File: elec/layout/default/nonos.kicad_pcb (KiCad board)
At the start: 2 copper layers, 60 parts, among them CN1 HRSHirose_DF40C_100DS_0_4V51, CN2 HRSHirose_DF40C_100DS_0_4V51, Q1 MOSFET, U1 STUSB4500QTR, U2 _Texas_Instruments_SN74LVC1G0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, U3 _Texas_Instruments_TAS5825MRH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, U4 Texas_Instruments_TPS56637RPAR

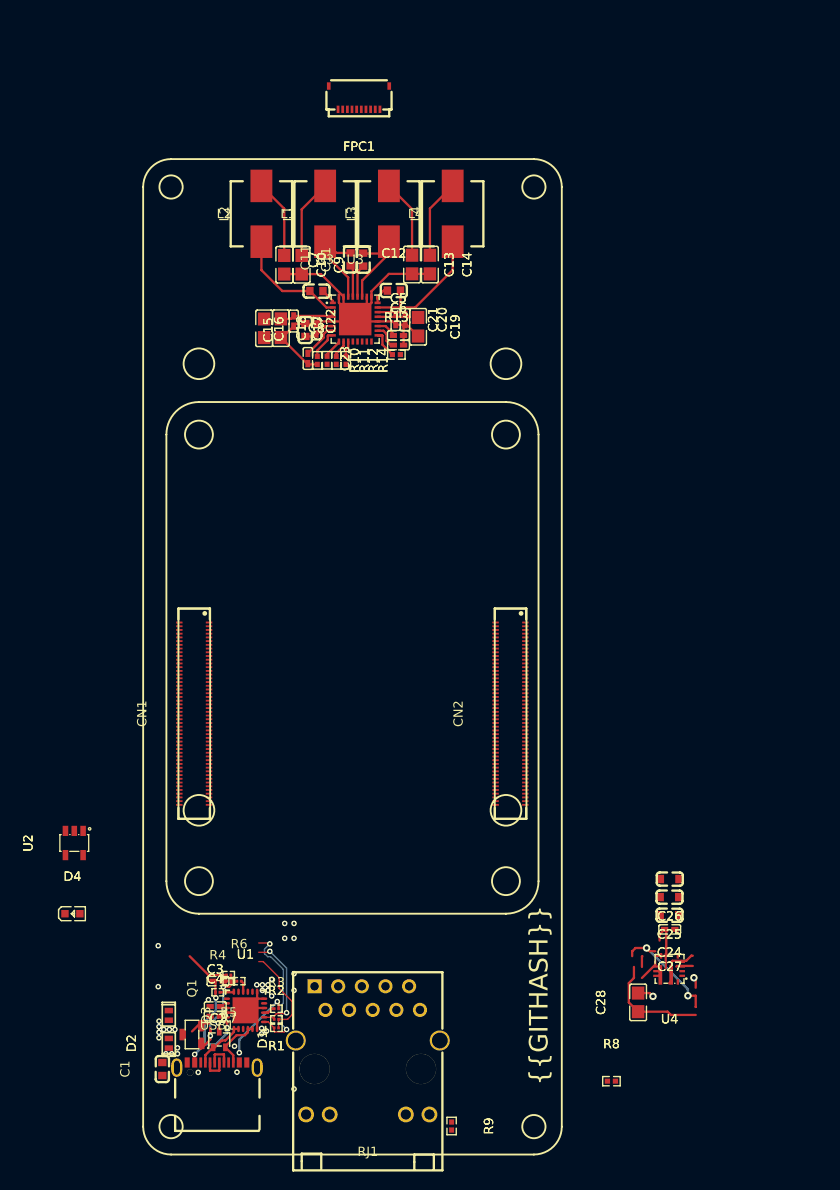
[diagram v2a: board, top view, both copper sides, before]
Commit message: add hat interface to nonos board
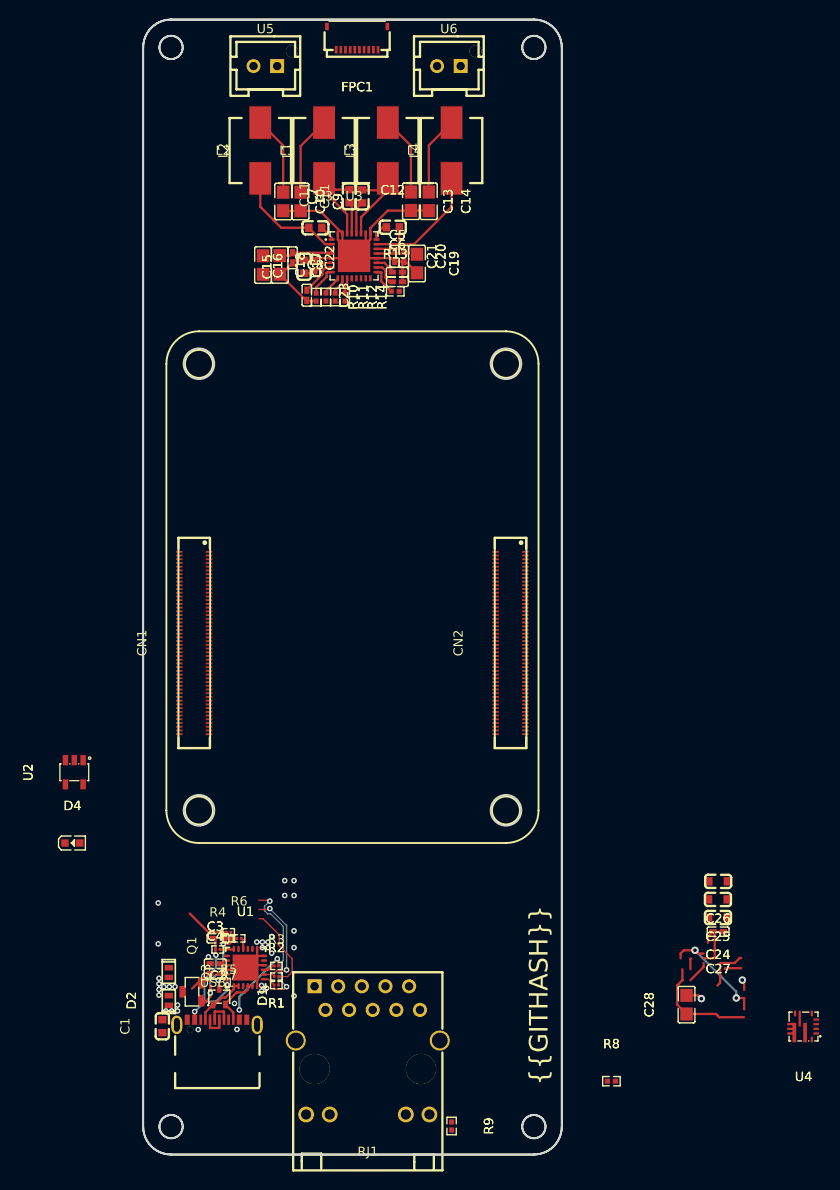
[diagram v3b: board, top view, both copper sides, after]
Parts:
- added U5: JST_Sales_America_B02B_XASK_1_ALFSN, lcsc:CONN-TH_B02B-XASK-1-A-LF-SN, F.Cu at (129.7, 49.4)
- added U6: JST_Sales_America_B02B_XASK_1_ALFSN, lcsc:CONN-TH_B02B-XASK-1-A-LF-SN, F.Cu at (149.5, 49.4)
- C5: value 1µF ±10% 25V X5R -> (none)
- C6: value (none) -> 1µF ±10% 25V X5R
- moved U4 15.7 mm to (187.6, 152.6)
- moved D4 7.60 mm to (109.0, 132.9)
- moved CN1 7.60 mm to (122.1, 111.4)
- moved CN2 7.60 mm to (156.1, 111.4)
- moved U2 7.60 mm to (109.2, 125.3)
- moved C17 6.80 mm to (131.3, 70.8)
- moved C18 6.80 mm to (129.5, 70.8)
- moved C5 6.80 mm to (143.9, 71.6)
- moved L1 6.80 mm to (136.0, 58.5)
- moved C10 6.80 mm to (131.7, 64.0)
- moved C13 6.80 mm to (145.4, 63.9)
- moved C9 6.80 mm to (133.5, 64.0)
- moved L2 6.80 mm to (129.2, 58.5)
- moved L3 6.80 mm to (142.9, 58.5)
- moved L4 6.80 mm to (149.8, 58.5)
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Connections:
- net amplifier-signal renamed net-2
- net amplifier-signal-1 renamed net-1
- net amplifier-signal-3 renamed net-3
- net pins[27] renamed processor.hdi_b-pins[27]
- net pins[38] renamed processor.hdi_b-pins[38]
- net pins[39] renamed processor.hdi_b-pins[39]
- net pins[46] renamed processor-pins[46]
- net processor-signal-7 renamed processor-pins[27]
- net processor-signal-8 renamed processor-pins[38]
- net processor.hdi_b-pins[28] renamed pins[28]
- C10 pad 2: amplifier-net -> amplifier-net-6
- C11 pad 1: amplifier-net-12 -> amplifier-net-4
- C11 pad 2: amplifier-net-9 -> amplifier-net-12
- C12 pad 1: amplifier-net-10 -> amplifier-net-1
- C12 pad 2: amplifier-net-4 -> amplifier-net-2
- C13 pad 2: amplifier-net -> amplifier-net-6
- C14 pad 2: amplifier-net -> amplifier-net-6
- C15 pad 2: amplifier-net -> amplifier-net-6
- C16 pad 2: amplifier-net -> amplifier-net-6
- C17 pad 2: amplifier-net -> amplifier-net-6
- C18 pad 2: amplifier-net -> amplifier-net-6
- C19 pad 2: amplifier-net -> amplifier-net-6
- C20 pad 2: amplifier-net -> amplifier-net-6
- C21 pad 2: amplifier-net -> amplifier-net-6
- C22 pad 2: amplifier-net -> amplifier-net-6
- C23 pad 1: amplifier-net-6 -> amplifier-net-8
- C23 pad 2: amplifier-net -> amplifier-net-6
- C5 pad 2: amplifier-net -> amplifier-net-6
- C6 pad 1: amplifier-net-3 -> amplifier-net-11
- C6 pad 2: amplifier-net -> amplifier-net-6
- C7 pad 1: amplifier-net-11 -> amplifier-net-5
- C7 pad 2: amplifier-net-5 -> amplifier-net
- C8 pad 1: amplifier-net-8 -> amplifier-net-10
- C8 pad 2: amplifier-net-1 -> amplifier-net-3
- C9 pad 1: amplifier-signal-2 -> net
- C9 pad 2: amplifier-net -> amplifier-net-6
- CN1 pad 15: signal-3 -> signal-6
- CN1 pad 17: signal-5 -> signal-7
- CN1 pad 19: pins[37] -> processor-signal-1
- CN1 pad 20: processor-signal-6 -> processor-pins[39]
- CN1 pad 23: pins[45] -> processor-signal-5
- CN1 pad 25: processor-signal-2 -> processor-signal-3
- CN1 pad 27: signal-2 -> signal-4
- CN1 pad 28: signal-6 -> signal-3
- CN1 pad 73: processor-signal-1 -> pins[54]
- CN1 pad 77: processor-signal-5 -> processor-pins[46]-1
- CN1 pad 78: processor-signal-4 -> processor-signal
- CN1 pad 82: signal-4 -> signal-5
- CN1 pad 85: processor-signal-3 -> processor-signal-2
- CN1 pad 86: processor-pins[28] -> processor-signal-4
- CN1 pad 87: processor-signal -> processor-signal-6
- D4 pad 1: net -> net-4
- FPC1 pad 10: signal-4 -> signal-5
- FPC1 pad 7: signal-2 -> signal-4
- FPC1 pad 8: signal-5 -> signal-7
- FPC1 pad 9: signal-3 -> signal-6
- L1 pad 1: amplifier-net-5 -> amplifier-net
- L1 pad 2: amplifier-signal-2 -> net
- L2 pad 1: amplifier-net-1 -> amplifier-net-3
- L3 pad 1: amplifier-net-9 -> amplifier-net-12
- L4 pad 1: amplifier-net-4 -> amplifier-net-2
- R10 pad 1: amplifier-net-2 -> amplifier-net-9
- R10 pad 2: amplifier-net -> amplifier-net-6
- R12 pad 1: signal-7 -> signal
- R13 pad 1: signal-6 -> signal-3
- R14 pad 1: signal -> signal-2
- R4 pad 2: pd_controller-net-3 -> pd_controller-net-2
- R6 pad 2: pd_controller-net-2 -> pd_controller-net-3
- R8 pad 2: rj45-net -> rj45-net-1
- R9 pad 2: rj45-net-1 -> rj45-net
- RJ1 pad 12: rj45-net -> rj45-net-1
- RJ1 pad 13: rj45-net-1 -> rj45-net
- U1 pad 16: pd_controller-net-2 -> pd_controller-net-3
- U1 pad 18: pd_controller-net-3 -> pd_controller-net-2
- U2 pad 4: net -> net-4
- U3 pad 1: amplifier-net-8 -> amplifier-net-10
- U3 pad 10: signal-7 -> signal
- U3 pad 11: signal -> signal-2
- U3 pad 17: signal-6 -> signal-3
- U3 pad 18: amplifier-net-3 -> amplifier-net-11
- U3 pad 2: amplifier-net-1 -> amplifier-net-3
- U3 pad 20: amplifier-net -> amplifier-net-6
- U3 pad 23: amplifier-net-4 -> amplifier-net-2
- U3 pad 24: amplifier-net-10 -> amplifier-net-1
- U3 pad 25: amplifier-net -> amplifier-net-6
- U3 pad 26: amplifier-net -> amplifier-net-6
- U3 pad 27: amplifier-net-9 -> amplifier-net-12
- U3 pad 28: amplifier-net-12 -> amplifier-net-4
- U3 pad 29: amplifier-net-11 -> amplifier-net-5
- U3 pad 30: amplifier-net-5 -> amplifier-net
- U3 pad 31: amplifier-net -> amplifier-net-6
- U3 pad 32: amplifier-net -> amplifier-net-6
- U3 pad 33: amplifier-net -> amplifier-net-6
- U3 pad 5: amplifier-net -> amplifier-net-6
- U3 pad 7: amplifier-net-6 -> amplifier-net-8
- U3 pad 8: amplifier-net-2 -> amplifier-net-9
- USB1 pad 5: pd_controller.USB_CONNECTOR-net-1 -> pd_controller.USB_CONNECTOR-net
- USB1 pad 6: pd_controller.USB_CONNECTOR-net -> pd_controller.USB_CONNECTOR-net-1
- USB1 pad 7: pd_controller.USB_CONNECTOR-net-1 -> pd_controller.USB_CONNECTOR-net
- USB1 pad 8: pd_controller.USB_CONNECTOR-net -> pd_controller.USB_CONNECTOR-net-1
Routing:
- net amplifier-net-6: track 12.4 -> 50.8 mm
- net amplifier-net-2: track 50.8 -> 14.6 mm
- net lv-1: track 20.0 -> 0.00 mm
- net lv: track 0.00 -> 20.0 mm, vias 1 -> 2
- net amplifier-net-11: track 14.6 -> 2.78 mm
- net pd_controller-net: track 12.1 -> 0.66 mm, vias 2 -> 0
- net pd_controller-net-1: track 1.22 -> 12.1 mm, vias 0 -> 2
- net amplifier-net-12: track 2.12 -> 10.8 mm
- net net: track 0.00 -> 8.52 mm
- net amplifier-signal-2: track 8.50 -> 0.00 mm
- net amplifier-net-3: track 4.03 -> 12.4 mm
- net amplifier-net-1: track 10.2 -> 2.12 mm
- net amplifier-net-5: track 10.8 -> 3.41 mm
- net amplifier-net: track 3.41 -> 10.2 mm
- net signal-5: track 3.34 -> 0.00 mm
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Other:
- board outline added: 45 x 122 mm

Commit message: builds working
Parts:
- removed USB1: TYPE_C_16PIN_2MD073, lcsc:USB-C-SMD_TYPE-C-6PIN-2MD-073
- added C29: 100nF ±10% 16V X7R, lcsc:C0402, F.Cu at (158.3, 151.4)
- added C30: 100pF ±5% 50V C0G, lcsc:C0402, F.Cu at (152.3, 150.9)
- added D5: , lcsc:LED0805-R-RD, F.Cu at (0.00, 0.00)
- added D6: , lcsc:LED0805-R-RD, F.Cu at (0.00, -5.00)
- added D7: , lcsc:LED0805-R-RD, F.Cu at (0.00, -10.0)
- added L5: 3.3µH ±20% 4A 73mΩ, lcsc:IND-SMD_L4.0-W4.0, F.Cu at (155.7, 155.4)
- added R15: 22kΩ ±1% 62.5mW, lcsc:R0402, F.Cu at (152.4, 152.0)
- added R16: 8.2kΩ ±1% 62.5mW, lcsc:R0402, F.Cu at (158.6, 154.7)
- added R17: 68kΩ ±1% 62.5mW, lcsc:R0402, F.Cu at (158.6, 156.8)
- added R18: 100kΩ ±1% 62.5mW, lcsc:R0402, F.Cu at (152.4, 153.2)
- added R19: 5.1kΩ ±1% 62.5mW, lcsc:R0402, F.Cu at (0.00, -15.0)
- added U7: _Texas_Instruments_TPS56637RPAR, lcsc:VQFN-HR-10_L3.0-W3.0_RPA, F.Cu at (155.6, 150.6)
- C10, C13, C14: value (none) -> 680nF ±10% 50V X7R
- C11, C12, C8: value (none) -> 470nF ±10% 50V X7R
- C18, C19: value (none) -> 22µF ±20% 25V X5R
- C2: value (none) -> 100nF ±10% 10V X5R; footprint lcsc:C0402 -> lcsc:C0201
- C20, C21, C22, C27: value (none) -> 100nF ±10% 16V X7R
- C23, C5: value (none) -> 1µF ±10% 25V X5R
- C24, C25, C26: value (none) -> 4.7µF ±10% 25V X5R; footprint lcsc:C0603 -> lcsc:C0805
- C3, C4: value (none) -> 1µF ±20% 6.3V X5R; footprint lcsc:C0402 -> lcsc:C0201
- D4: value 2.7V -> (none); footprint lcsc:LED0603-RD_WHITE -> lcsc:LED0805-R-RD
- L1, L3, L4: value (none) -> 10µH ±20% 4.5A 68mΩ
- Q1: footprint lcsc:SOT-23-3_L2.9-W1.3-P1.90-LS2.4-BR -> lcsc:SOT-23-3_L2.9-W1.3-P1.90-LS2.4-BR-1
- R1: value (none) -> 1kΩ ±1% 50mW
- R12, R13, R14: value (none) -> 10kΩ ±1% 62.5mW
- R2: value 4.64kΩ ±1% 50mW -> 4.7kΩ ±1% 50mW
- R3: value (none) -> 4.7kΩ ±1% 50mW
- R8: value 453Ω ±1% 62.5mW -> 470Ω ±1% 62.5mW
- R9: value (none) -> 470Ω ±1% 62.5mW
- U4: value Texas_Instruments_TPS56637RPAR -> _HCTL_HC_TYPE_C_24P_VS9_3_5A_F1_1_04; footprint lcsc:VQFN-HR-10_L3.0-W3.0_RPA -> lcsc:USB-C-SMD_HC-TYPE-C-24P-VS9.3-5A-F1.1-04; moved to B.Cu
- moved U4 48.7 mm to (139.1, 157.6), turned to -90 degrees
- moved R8 37.2 mm to (130.1, 163.5), turned to -90 degrees
- moved C25 23.3 mm to (155.8, 144.5)
- moved C26 23.3 mm to (155.8, 142.6)
- moved C27 23.3 mm to (155.8, 148.0)
- moved C24 23.3 mm to (155.8, 146.5)
- moved C28 23.3 mm to (152.4, 155.8)
- moved R1 14.3 mm to (122.3, 157.6), turned to 90 degrees
- moved R2 14.2 mm to (120.3, 157.6), turned to -90 degrees
- moved R3 14.2 mm to (121.2, 157.6), turned to -90 degrees
- moved R6 10.5 mm to (125.3, 153.6), turned to -90 degrees
- moved R5 9.95 mm to (125.9, 152.5), turned to 90 degrees
- moved U1 9.65 mm to (122.1, 154.3), turned to -90 degrees
- moved R7 9.33 mm to (125.3, 152.5), turned to 90 degrees
- moved C2 8.17 mm to (125.3, 151.3), turned to 90 degrees
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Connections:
- net pins[47] renamed processor-signal-7
- net processor-pins[40] renamed processor-signal-8
- net processor.hdi_b-pins[40] renamed pins[40]
- C10 pad 1: net-1 -> net
- C10 pad 2: amplifier-net-6 -> lv
- C11 pad 1: amplifier-net-4 -> amplifier-net-6
- C11 pad 2: amplifier-net-12 -> amplifier-net-4
- C12 pad 1: amplifier-net-1 -> amplifier-net-5
- C12 pad 2: amplifier-net-2 -> amplifier-net-3
- C13 pad 1: net-3 -> net-4
- C13 pad 2: amplifier-net-6 -> lv
- C14 pad 2: amplifier-net-6 -> lv
- C15 pad 1: DVDD -> VCC_3V3
- C15 pad 2: amplifier-net-6 -> lv
- C16 pad 1: DVDD -> VCC_3V3
- C16 pad 2: amplifier-net-6 -> lv
- C17 pad 1: PVDD -> VSINK_VCC
- C17 pad 2: amplifier-net-6 -> lv
- C18 pad 1: PVDD -> VSINK_VCC
- C18 pad 2: amplifier-net-6 -> lv
- C19 pad 1: PVDD -> VSINK_VCC
- C19 pad 2: amplifier-net-6 -> lv
- C2 pad 1: pd_controller-net -> pd_controller-net-2
- C20 pad 1: PVDD -> VSINK_VCC
- C20 pad 2: amplifier-net-6 -> lv
- C21 pad 1: PVDD -> VSINK_VCC
- C21 pad 2: amplifier-net-6 -> lv
- C22 pad 1: PVDD -> VSINK_VCC
- C22 pad 2: amplifier-net-6 -> lv
- C23 pad 2: amplifier-net-6 -> lv
- C28 pad 1: hv -> net-3
- C5 pad 2: amplifier-net-6 -> lv
- C6 pad 1: amplifier-net-11 -> amplifier-net-9
- C6 pad 2: amplifier-net-6 -> lv
- C7 pad 1: amplifier-net-5 -> amplifier-net-10
- C7 pad 2: amplifier-net -> amplifier-net-2
- C8 pad 1: amplifier-net-10 -> amplifier-net
- C8 pad 2: amplifier-net-3 -> amplifier-net-1
- C9 pad 1: net -> net-1
- C9 pad 2: amplifier-net-6 -> lv
- CN1 pad 15: signal-6 -> signal-1
- CN1 pad 17: signal-7 -> signal-3
- CN1 pad 19: processor-signal-1 -> processor-signal-5
- CN1 pad 23: processor-signal-5 -> processor-signal
- CN1 pad 28: signal-3 -> signal-5
- CN1 pad 29: signal-1 -> signal-6
- CN1 pad 73: pins[54] -> processor-signal-1
- CN1 pad 77: processor-pins[46]-1 -> processor-pins[46]
- CN1 pad 78: processor-signal -> processor-signal-4
- CN1 pad 82: signal-5 -> signal-2
- CN1 pad 85: processor-signal-2 -> pins[30]
- CN1 pad 86: processor-signal-4 -> processor-signal-6
- CN1 pad 87: processor-signal-6 -> processor-signal-2
- CN2 pad 77: processor-pins[46] -> processor-pins[46]-1
- D4 pad 1: net-4 -> processor-net
- D4 pad 2: VCC_3V3 -> processor-net-1
- FPC1 pad 10: signal-5 -> signal-2
- FPC1 pad 4: hv -> net-3
- FPC1 pad 6: lv-1 -> lv
- FPC1 pad 8: signal-7 -> signal-3
- FPC1 pad 9: signal-6 -> signal-1
- L1 pad 1: amplifier-net -> amplifier-net-2
- L1 pad 2: net -> net-1
- L2 pad 1: amplifier-net-3 -> amplifier-net-1
- L2 pad 2: net-1 -> net
- L3 pad 1: amplifier-net-12 -> amplifier-net-4
- L3 pad 2: net-3 -> net-4
- L4 pad 1: amplifier-net-2 -> amplifier-net-3
- Q1 pad 1: pd_controller-net-1 -> pd_controller-net
- R10 pad 1: amplifier-net-9 -> amplifier-net-11
- R10 pad 2: amplifier-net-6 -> lv
- R11 pad 1: signal-1 -> signal-6
- R12 pad 1: signal -> signal-7
- R13 pad 1: signal-3 -> signal-5
- R14 pad 1: signal-2 -> signal
- R2 pad 2: pd_controller-hv -> hv
- R3 pad 2: pd_controller-hv -> hv
- R4 pad 2: pd_controller-net-2 -> pd_controller-net-1
- R5 pad 1: pd_controller-net-1 -> pd_controller-net
- R6 pad 1: pd_controller-net-1 -> pd_controller-net
- R7 pad 1: pd_controller-net-1 -> pd_controller-net
- R7 pad 2: pd_controller-net -> pd_controller-net-2
- RJ1 pad SHIELD0: lv-1 -> lv
- RJ1 pad SHIELD1: lv-1 -> lv
- U1 pad 18: pd_controller-net-2 -> pd_controller-net-1
- U2 pad 4: net-4 -> processor-net
- U3 pad 1: amplifier-net-10 -> amplifier-net
- U3 pad 10: signal -> signal-7
- U3 pad 11: signal-2 -> signal
- U3 pad 17: signal-3 -> signal-5
- U3 pad 18: amplifier-net-11 -> amplifier-net-9
- U3 pad 2: amplifier-net-3 -> amplifier-net-1
- U3 pad 20: amplifier-net-6 -> lv
- U3 pad 21: PVDD -> VSINK_VCC
- U3 pad 22: PVDD -> VSINK_VCC
- U3 pad 23: amplifier-net-2 -> amplifier-net-3
- U3 pad 24: amplifier-net-1 -> amplifier-net-5
- U3 pad 25: amplifier-net-6 -> lv
- U3 pad 26: amplifier-net-6 -> lv
- U3 pad 27: amplifier-net-12 -> amplifier-net-4
- U3 pad 28: amplifier-net-4 -> amplifier-net-6
- U3 pad 29: amplifier-net-5 -> amplifier-net-10
- U3 pad 3: PVDD -> VSINK_VCC
- U3 pad 30: amplifier-net -> amplifier-net-2
- U3 pad 31: amplifier-net-6 -> lv
- U3 pad 32: amplifier-net-6 -> lv
- U3 pad 33: amplifier-net-6 -> lv
- U3 pad 4: PVDD -> VSINK_VCC
- U3 pad 5: amplifier-net-6 -> lv
- U3 pad 6: DVDD -> VCC_3V3
- U3 pad 8: amplifier-net-9 -> amplifier-net-11
- U3 pad 9: signal-1 -> signal-6
- U5 pad 1: net-1 -> net
- U5 pad 2: net -> net-1
- U6 pad 1: net-2 -> net-4
- U6 pad 2: net-3 -> net-2
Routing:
- net amplifier-net-6: track 50.8 -> 1.70 mm
- net lv: track 20.0 -> 59.2 mm
- net VBUS: track 24.6 -> 0.00 mm, vias 11 -> 0
- net net-4: track 0.00 -> 17.4 mm
- net I2C_SCL: track 15.2 -> 0.00 mm, vias 2 -> 0
- net PVDD: track 14.5 -> 0.00 mm
- net regulator-net-3: track 0.00 -> 12.3 mm, vias 0 -> 2
- net I2S_WS: track 12.3 -> 0.00 mm, vias 2 -> 0
- net pd_controller-net-1: track 12.1 -> 0.00 mm, vias 2 -> 0
- net hv: track 11.8 -> 0.00 mm
- net I2C_SDA: track 11.6 -> 0.00 mm, vias 2 -> 0
- net amplifier-net-5: track 3.41 -> 14.6 mm
- net amplifier-net-12: track 10.8 -> 0.00 mm
- net amplifier-net-7: track 2.20 -> 12.4 mm
- net pd_controller-hv: track 10.1 -> 0.00 mm
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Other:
- board text removed: "USBPD DEV BOARD"
